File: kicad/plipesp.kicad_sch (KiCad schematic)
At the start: 33 parts, among them CON1 IEEEE-1284A, J1 USB_B_Micro, J2 Conn_01x04_Male, J3 Conn_01x06_Male, J4 Micro_SD_Card_Det, U1 AMS1117-3.3, U2 CBTD3384, U3 CBTD3384, U4 ESP32-WROOM-32D

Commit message: rev3s - with SD card
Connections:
- net BUSY: now also U4.11 (IO26); no longer U4.8 (IO32)
- net POUT: now also U4.9 (IO33); no longer U4.11 (IO26)
- net ~{AMI_RESET}: now also U4.8 (IO32); no longer U4.9 (IO33)

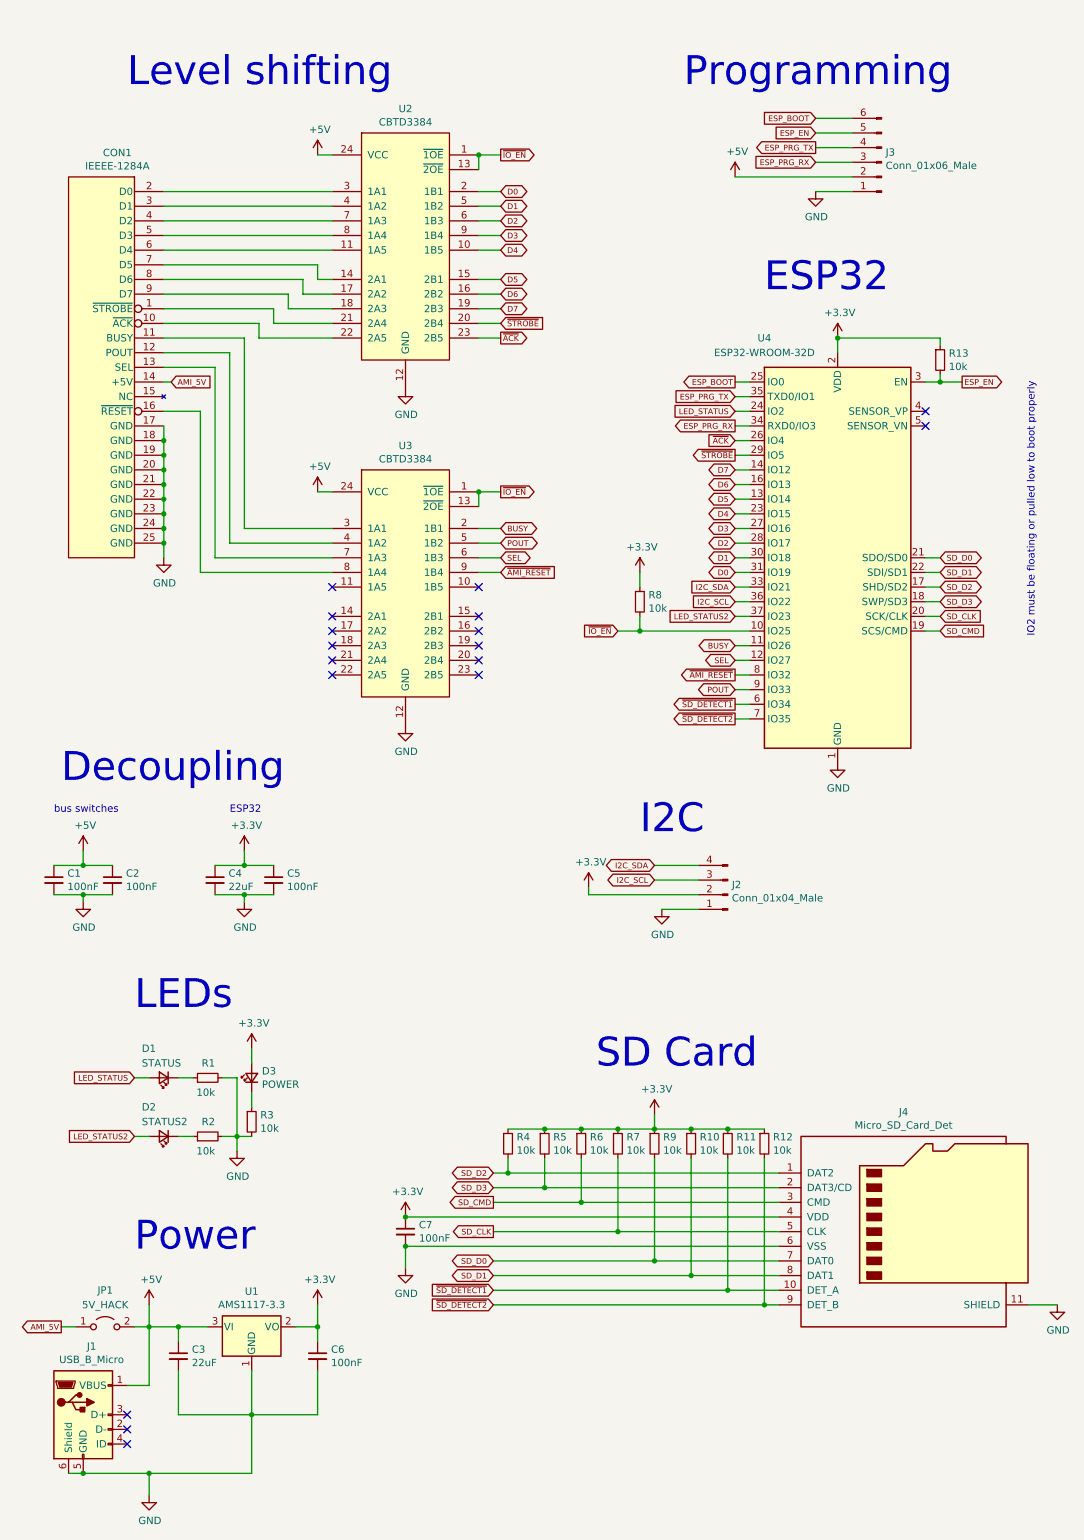
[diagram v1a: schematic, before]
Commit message: rev3 - without SD card, AMI_RESET optional, extra IO on pins
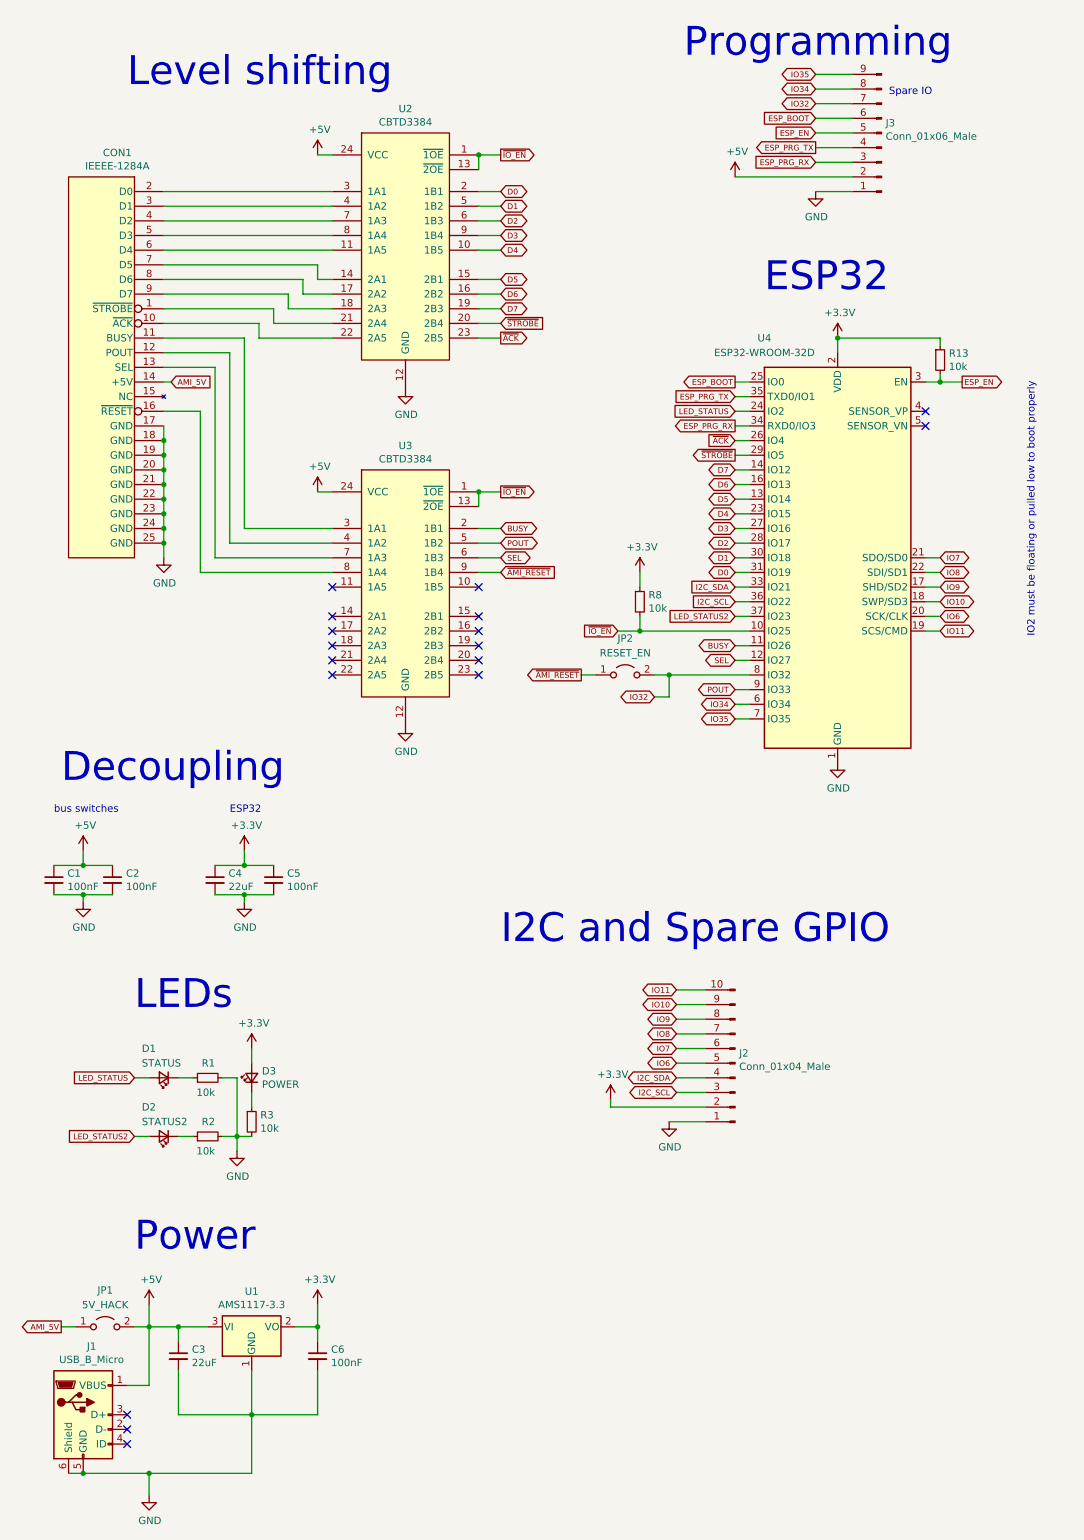
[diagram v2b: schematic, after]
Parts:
- removed C7: 100nF, Capacitor_SMD:C_0805_2012Metric, symbol Device:C_Small
- removed J4: Micro_SD_Card_Det, Connector_Card:microSD_HC_Hirose_DM3D-SF, symbol Connector:Micro_SD_Card_Det
- removed R10, R11, R12, R4, R5, R6, R7, R9: 10k, Resistor_SMD:R_0805_2012Metric, symbol Device:R_Small
- added JP2: RESET_EN, Jumper:SolderJumper-2_P1.3mm_Open_RoundedPad1.0x1.5mm, symbol Jumper:Jumper_2_Open
- J2: footprint Connector_PinHeader_2.54mm:PinHeader_1x04_P2.54mm_Vertical -> Connector_PinHeader_2.54mm:PinHeader_1x10_P2.54mm_Vertical; symbol Connector:Conn_01x04_Male -> Connector:Conn_01x10_Male
- J3: footprint Connector_PinHeader_2.54mm:PinHeader_1x06_P2.54mm_Vertical -> Connector_PinHeader_2.54mm:PinHeader_1x09_P2.54mm_Vertical; symbol Connector:Conn_01x06_Male -> Connector:Conn_01x09_Male
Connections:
- net ~{AMI_RESET}: now also JP2.1 (A); no longer U4.8 (IO32)
- net SD_CLK renamed IO6
- net IO6: now also J2.5 (Pin_5)
- net SD_CMD renamed IO11
- net IO11: now also J2.10 (Pin_10)
- net SD_D0 renamed IO7
- net IO7: now also J2.6 (Pin_6)
- net SD_D1 renamed IO8
- net IO8: now also J2.7 (Pin_7)
- net SD_D2 renamed IO9
- net IO9: now also J2.8 (Pin_8)
- net SD_D3 renamed IO10
- net IO10: now also J2.9 (Pin_9)
- net ~{SD_DETECT1} renamed IO34
- net IO34: now also J3.8 (Pin_8)
- net ~{SD_DETECT2} renamed IO35
- net IO35: now also J3.9 (Pin_9)
- new net IO32: J3.7 (Pin_7), JP2.2 (B), U4.8 (IO32)
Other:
- note added: "I2C and Spare GPIO"
- note added: "Spare IO"
- note removed: "I2C"
- note removed: "SD Card"
